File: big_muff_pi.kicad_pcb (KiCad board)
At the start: 2 copper layers, 63 parts, among them J1 NMJ6HHD2, J2 NMJ6HHD2, Q1 MMBT5551, Q2 MMBT5551, Q3 MMBT5551, Q4 MMBT5551, Q5 MMBT5551, SW1 SW_DPDT_x2

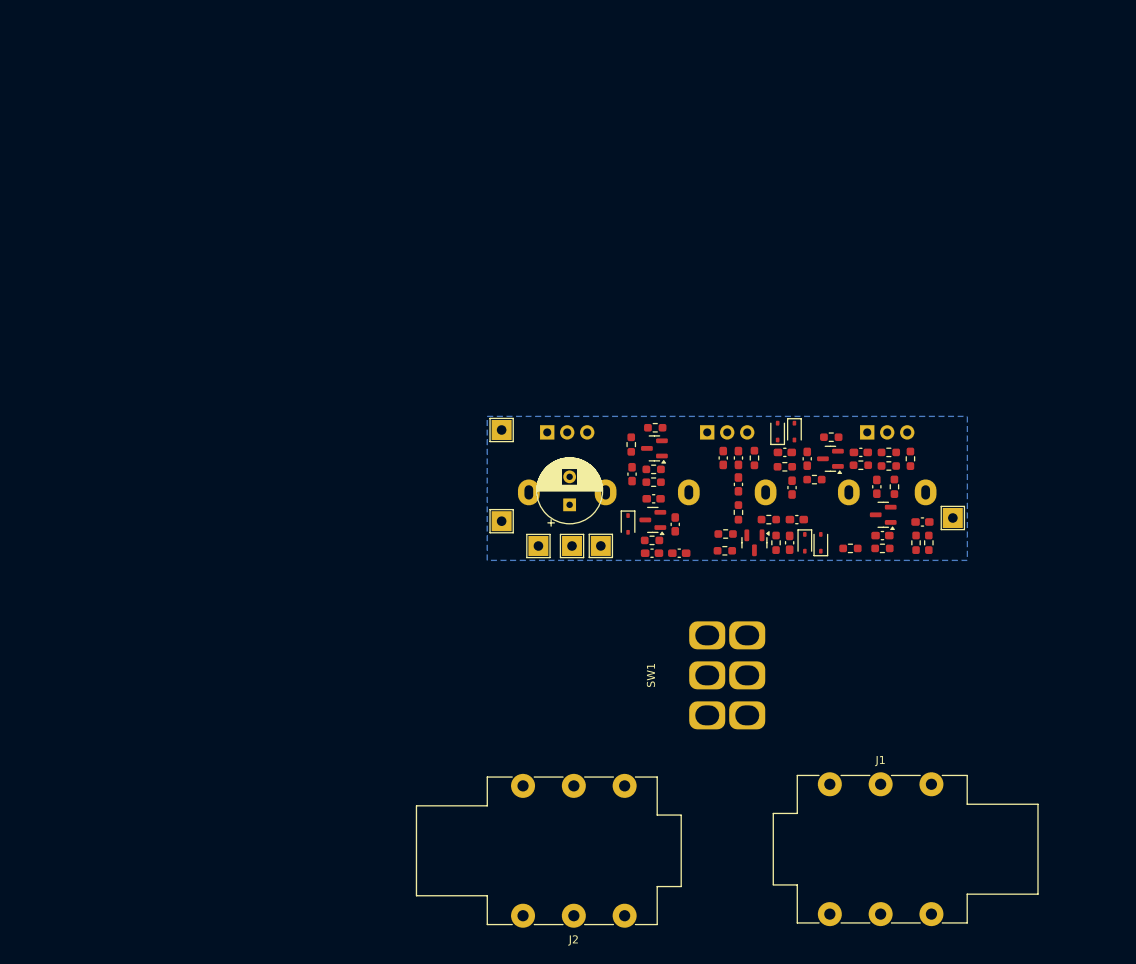
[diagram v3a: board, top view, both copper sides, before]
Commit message: 3D bodies
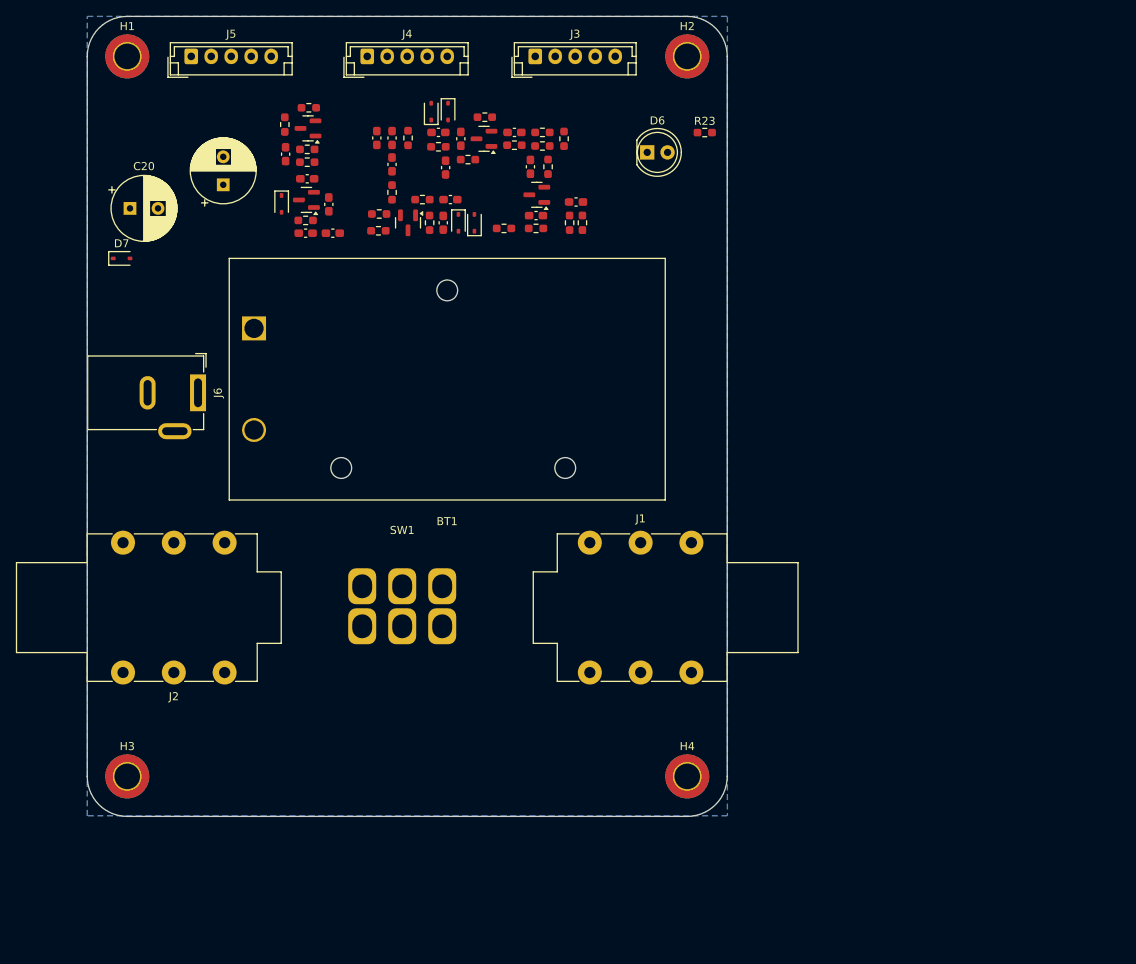
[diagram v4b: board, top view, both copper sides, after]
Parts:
- removed RV1, RV2, RV3: 100k, Potentiometer_THT:Potentiometer_Alpha_RD901F-40-00D_Single_Vertical
- removed TP11: input, TestPoint:TestPoint_THTPad_2.5x2.5mm_Drill1.2mm
- removed TP12, TP14: ground, TestPoint:TestPoint_THTPad_2.5x2.5mm_Drill1.2mm
- removed TP15: SW_OFF, TestPoint:TestPoint_THTPad_2.5x2.5mm_Drill1.2mm
- removed TP16: SW_ON, TestPoint:TestPoint_THTPad_2.5x2.5mm_Drill1.2mm
- removed TP4: SW_MID, TestPoint:TestPoint_THTPad_2.5x2.5mm_Drill1.2mm
- added BT1: Battery_Cell, pedale:BatteryHolder_Eagle_12BH611-GR, F.Cu at (70.8, 89.0)
- added C20: 470u, Capacitor_THT:CP_Radial_D8.0mm_P3.50mm, F.Cu at (55.3, 74.0)
- added D6: LED, LED_THT:LED_D5.0mm, F.Cu at (120.0, 67.0)
- added D7: 1N4148WS, Diode_SMD:D_SOD-323, F.Cu at (54.3, 80.2)
- added H1: MountingHole, pedale:M3_hole_with_spacer, F.Cu at (55.0, 55.0)
- added H2: MountingHole, pedale:M3_hole_with_spacer, F.Cu at (125.0, 55.0)
- added H3: MountingHole, pedale:M3_hole_with_spacer, F.Cu at (55.0, 145.0)
- added H4: MountingHole, pedale:M3_hole_with_spacer, F.Cu at (125.0, 145.0)
- added J3: Conn_01x05, Connector_JST:JST_EH_B5B-EH-A_1x05_P2.50mm_Vertical, F.Cu at (106.0, 55.0)
- added J4: Conn_01x05, Connector_JST:JST_EH_B5B-EH-A_1x05_P2.50mm_Vertical, F.Cu at (85.0, 55.0)
- added J5: Conn_01x05, Connector_JST:JST_EH_B5B-EH-A_1x05_P2.50mm_Vertical, F.Cu at (63.0, 55.0)
- added J6: Barrel_Jack_MountingPin, Connector_BarrelJack:BarrelJack_GCT_DCJ200-10-A_Horizontal, F.Cu at (63.9, 97.0)
- added R23: 1k, Resistor_SMD:R_0603_1608Metric_Pad0.98x0.95mm_HandSolder, F.Cu at (127.2, 64.5)
- moved D3 58.9 mm to (95.1, 61.9)
- moved D5 58.9 mm to (93.0, 61.9)
- moved C1 58.9 mm to (106.1, 74.9)
- moved C12 58.9 mm to (88.1, 68.5)
- moved C13 58.9 mm to (88.1, 65.2)
- moved C2 58.9 mm to (111.1, 73.2)
- moved C9 58.9 mm to (94.5, 75.8)
- moved Q1 58.9 mm to (99.6, 65.3)
- moved Q2 58.9 mm to (90.1, 75.8)
- moved Q3 58.9 mm to (77.6, 64.0)
- moved R16 58.9 mm to (86.5, 74.7)
- moved R17 58.9 mm to (90.1, 65.2)
- moved R2 58.9 mm to (107.6, 68.8)
- moved R22 58.9 mm to (88.1, 72.0)
- moved R4 58.9 mm to (106.1, 76.5)
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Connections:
- C10 pad 1: Net-(C10-Pad1) -> F_OUT
- C3 pad 2: Net-(C3-Pad2) -> FS_OUT
- J1 pad T: Net-(J1-PadT) -> SW_IN
- J2 pad T: Net-(J2-PadT) -> Net-(SW1A-B)
- R3 pad 1: Net-(J1-PadT) -> SW_IN
- SW1 pad 1: unconnected-(SW1A-A-Pad1) -> Net-(J5-Pin_3)
- SW1 pad 2: unconnected-(SW1A-B-Pad2) -> Net-(SW1A-B)
- SW1 pad 3: unconnected-(SW1A-C-Pad3) -> SW_IN
- SW1 pad 4: unconnected-(SW1B-A-Pad4) -> 9V
- SW1 pad 5: unconnected-(SW1B-B-Pad5) -> Net-(D6-A)
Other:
- board outline added: 80 x 100 mm
